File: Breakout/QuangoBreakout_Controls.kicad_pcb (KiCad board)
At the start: 2 copper layers, 18.8 x 110 mm, 36 parts, among them J1 Audio_Send_A, J10 Audio_Breakout, J2 Audio_Send_B, J3 Audio_Return_A, J4 Audio_Return_A, J6 Eurorack_10_pin_power, J7 JackMixA, J8 JackMixB, J9 JackMixBoth, U1 TL074

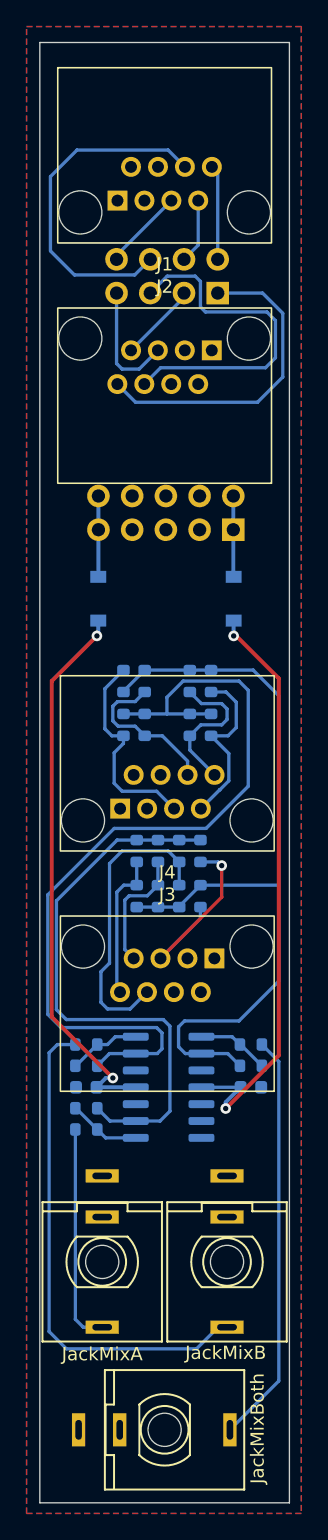
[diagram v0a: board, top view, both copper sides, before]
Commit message: Updated to Kicad 7.05
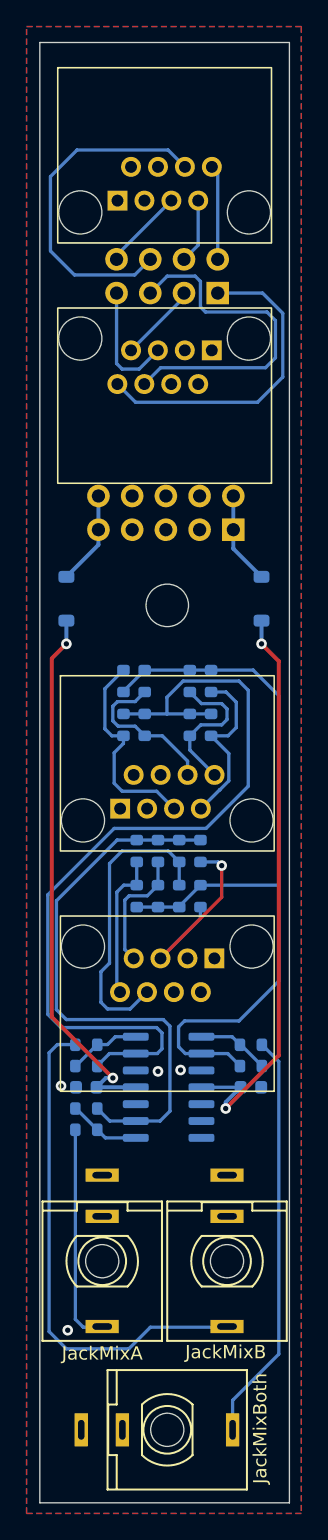
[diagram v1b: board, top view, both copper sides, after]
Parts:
- added H1: MountingHole, MountingHole:MountingHole_3.2mm_M3_ISO14580, F.Cu at (59.6, 92.4)
- moved D1 2.40 mm to (52.0, 91.9)
- moved D2 2.10 mm to (66.7, 91.9)
- moved J9 0.20 mm to (59.6, 154.5)
- moved J7 0.05 mm to (54.7, 141.8)
- moved J8 0.05 mm to (64.1, 141.8)
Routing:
- net /+12V_IN: track 6.10 -> 7.09 mm
- net +12V: track 42.3 -> 41.3 mm
- net -12V: track 44.9 -> 44.0 mm
- net /-12V_IN: track 6.10 -> 6.97 mm
- net GND: vias 0 -> 4
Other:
- board text added: "-12V"
- board text added: "A1"
- board text added: "A4"
- board text added: "Audio In"
- board text added: "B1"
- board text added: "B4"
- board text added: "Mountjoy Modular"
- board text added: "Power"
- board text added: "Quango Breakout v1.0 2023"
- board text removed: "QBreakout v1.0"
